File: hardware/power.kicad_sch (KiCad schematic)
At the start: 27 parts, among them J7 12401610E4#2A, Q1 DMG2307L, Q2 DMG2307L, Q3 BSD235N, U7 AP9101CK, U8 MIC5504-3.3YM5

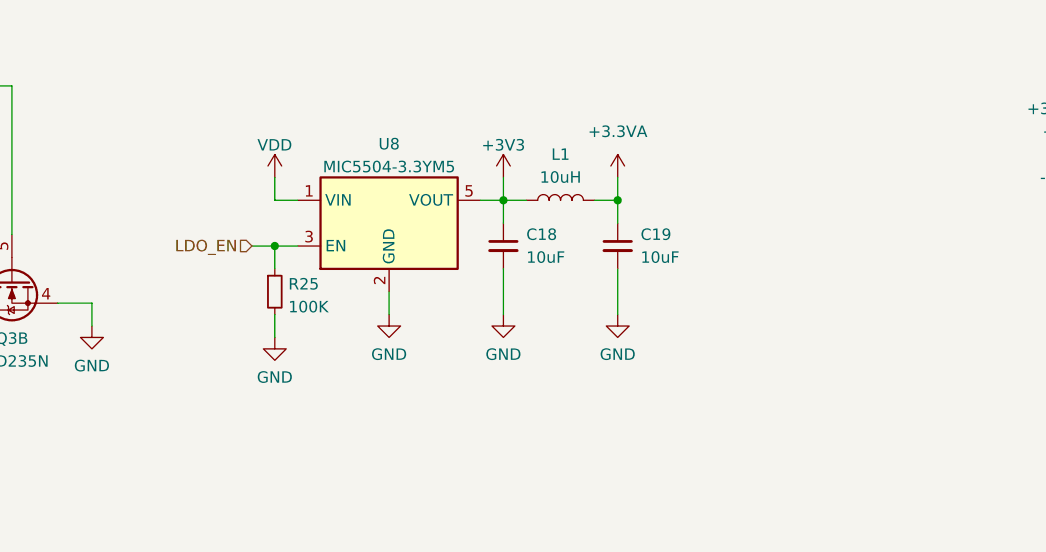
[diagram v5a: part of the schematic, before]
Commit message: Added solder bridges and calculated resistor values for INA
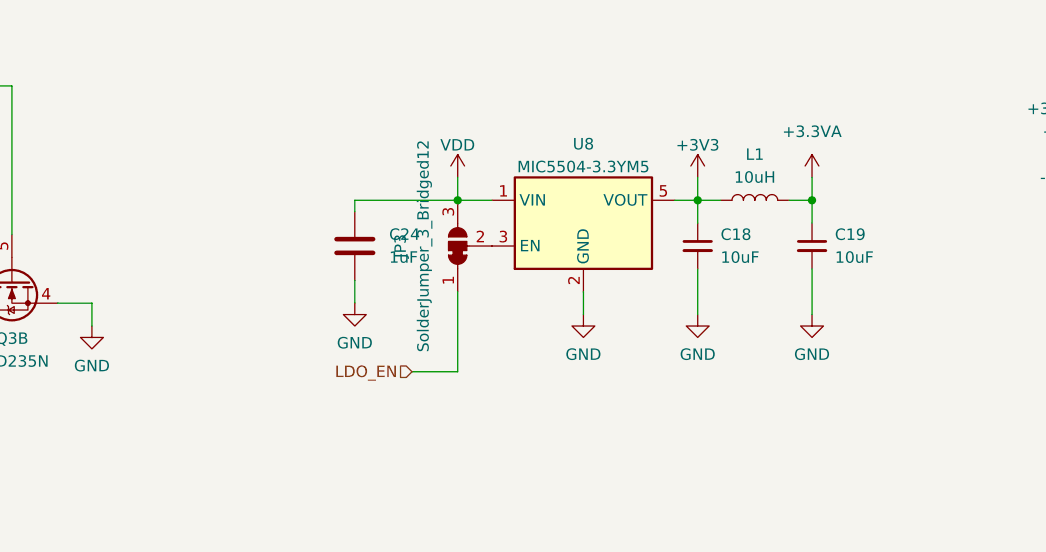
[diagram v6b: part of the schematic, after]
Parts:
- removed R25: 100K, Resistor_SMD:R_0603_1608Metric, symbol Device:R_Small
- added C24: 1uF, Capacitor_SMD:C_0603_1608Metric, symbol Device:C
- added JP3: SolderJumper_3_Bridged12, symbol Jumper:SolderJumper_3_Bridged12
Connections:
- net +BATT: now also C24.2, JP3.3 (B)
- net GND: now also C24.1
- net LDO_EN: now also JP3.1 (A); no longer U8.3 (EN)
- new net: JP3.2 (C), U8.3 (EN)
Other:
- moved on the sheet: C18, C19, L1, U8

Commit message: Set jumper footprints and updated design rules for Oshpark After Dark
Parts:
- JP3: footprint (none) -> Jumper:SolderJumper-3_P1.3mm_Bridged2Bar12_RoundedPad1.0x1.5mm
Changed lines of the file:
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@@
 			)
 		)
-		(property "Footprint" ""
+		(property "Footprint" "Jumper:SolderJumper-3_P1.3mm_Bridged2Bar12_RoundedPad1.0x1.5mm"
 			(at 193.04 36.83 0)
 			(effects

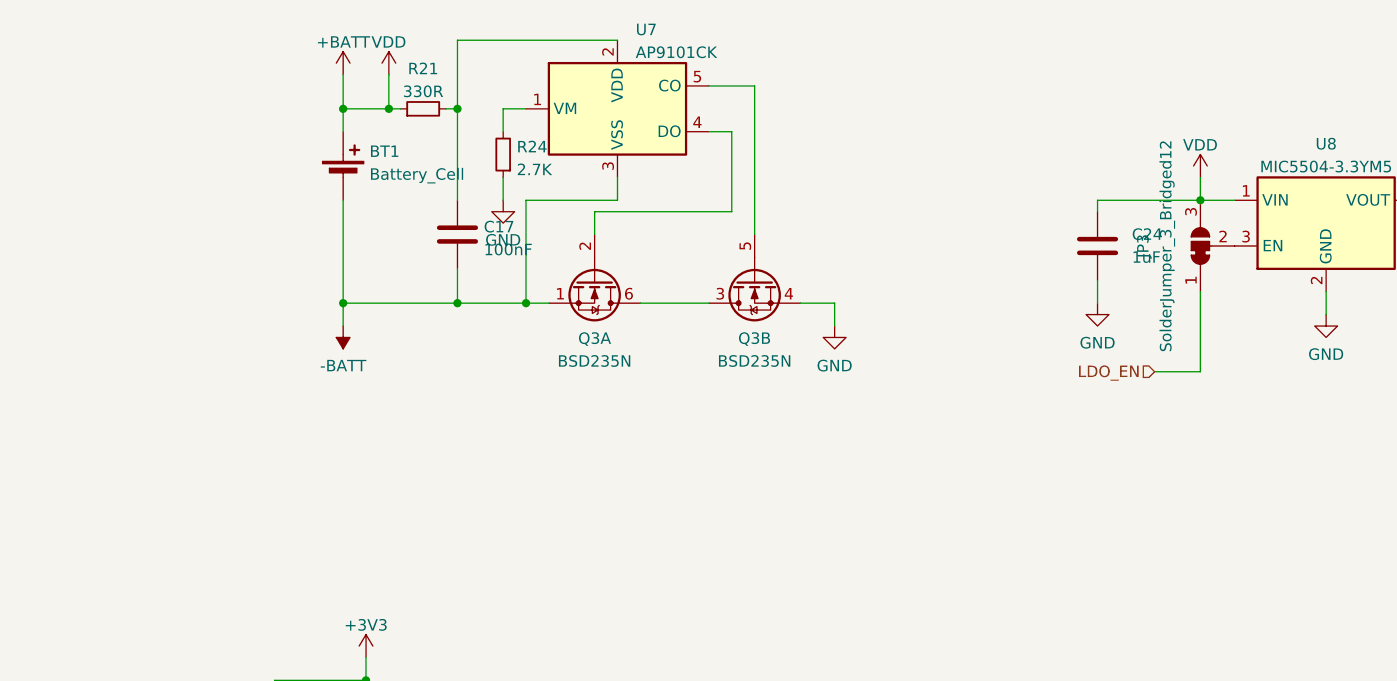
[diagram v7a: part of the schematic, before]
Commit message: Realized that 5V to VBat pin would fry the uC and abandoned ultra-low power design. Deferred to next revision.
A
A
A
A
A
A
A
A
A
A
A
A
A
A
A
A
A
A
B
B
B
B
B
B
B
B
B
B
B
B
B
B
B
A
A
A
A
A
A
A
A
A
A
A
A
A
A
P
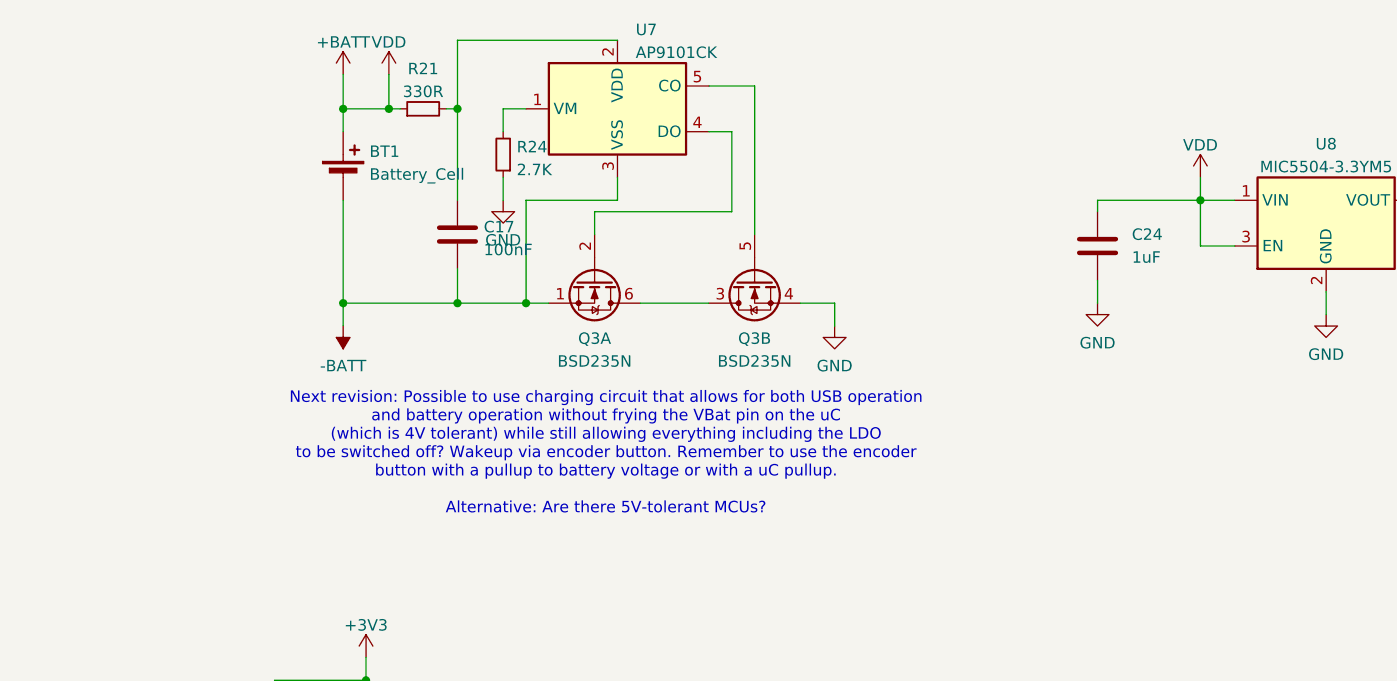
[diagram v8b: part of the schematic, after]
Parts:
- removed JP3: SolderJumper_3_Bridged12, Jumper:SolderJumper-3_P1.3mm_Bridged2Bar12_RoundedPad1.0x1.5mm, symbol Jumper:SolderJumper_3_Bridged12
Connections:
- net +BATT: now also U8.3 (EN)
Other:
- note added: "Next revision: Possible to use charging circuit that allows for both USB operation and battery operation without frying the VBat pin on the uC (which is 4V tolerant) while still allowing everything including the LDO to be switched off? Wakeup via encoder button. Remember to use the encoder button with a pullup to battery voltage or with a uC pullup. Alternative: Are there 5V-tolerant MCUs?"
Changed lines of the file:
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@@
 	(generator_version "9.0")
 	(paper "A4")
+	(text "Next revision: Possible to use charging circuit that allows for both USB operation \nand battery operation without frying the VBat pin on the uC \n(which is 4V tolerant) while still allowing everything including the LDO \nto be switched off? Wakeup via encoder button. Remember to use the encoder \nbutton with a pullup to battery voltage or with a uC pullup. \n\nAlternative: Are there 5V-tolerant MCUs?"
+		(exclude_from_sim no)
+		(at 127 59.944 0)
+		(effects
+			(font
+				(size 1.27 1.27)
+			)
+		)
+	)
 	(junction
 		(at 193.04 31.75)
@@
 	(wire
 		(pts
-			(xy 193.04 41.91) (xy 193.04 50.8)
-		)
-		(stroke
-			(width 0)
-			(type default)
-		)
-	)
-	(wire
-		(pts
 			(xy 140.97 33.02) (xy 125.73 33.02)
 		)
@@
 	(wire
 		(pts
+			(xy 193.04 36.83) (xy 193.04 31.75)
+		)
+		(stroke
+			(width 0)
+			(type default)
+		)
+	)
+	(wire
+		(pts
 			(xy 110.49 39.37) (xy 110.49 43.18)
 		)
@@
 	(wire
 		(pts
-			(xy 138.43 19.05) (xy 143.51 19.05)
+			(xy 196.85 36.83) (xy 193.04 36.83)
 		)
 		(stroke
@@
 	(wire
 		(pts
-			(xy 138.43 24.13) (xy 140.97 24.13)
+			(xy 138.43 19.05) (xy 143.51 19.05)
 		)
 		(stroke
@@
 	(wire
 		(pts
-			(xy 207.01 41.91) (xy 207.01 44.45)
+			(xy 138.43 24.13) (xy 140.97 24.13)
 		)
 		(stroke
@@
 	(wire
 		(pts
-			(xy 90.17 132.08) (xy 90.17 129.54)
+			(xy 207.01 41.91) (xy 207.01 44.45)
 		)
 		(stroke
@@
 	(wire
 		(pts
-			(xy 181.61 33.02) (xy 181.61 31.75)
+			(xy 90.17 132.08) (xy 90.17 129.54)
 		)
 		(stroke
@@
 	(wire
 		(pts
-			(xy 80.01 95.25) (xy 82.55 95.25)
+			(xy 181.61 33.02) (xy 181.61 31.75)
 		)
 		(stroke
@@
 	(wire
 		(pts
-			(xy 128.27 13.97) (xy 110.49 13.97)
+			(xy 80.01 95.25) (xy 82.55 95.25)
 		)
 		(stroke
@@
 	(wire
 		(pts
-			(xy 187.96 50.8) (xy 193.04 50.8)
+			(xy 128.27 13.97) (xy 110.49 13.97)
 		)
 		(stroke
@@
 		)
 	)
-	(hierarchical_label "LDO_EN"
-		(shape input)
-		(at 187.96 50.8 180)
-		(effects
-			(font
-				(size 1.27 1.27)
-			)
-			(justify right)
-		)
-	)
 	(hierarchical_label "DISPLAY_POWER"
 		(shape output)
@@
 					(unit 1)
 				)
-			)
-		)
-	)
-	(symbol
-		(lib_id "Jumper:SolderJumper_3_Bridged12")
-		(at 193.04 36.83 90)
-		(unit 1)
-		(exclude_from_sim no)
-		(in_bom no)
-		(on_board yes)
-		(dnp no)
-		(property "Reference" "JP3"
-			(at 186.69 36.83 0)
-			(effects
-				(font
-					(size 1.27 1.27)
-				)
-			)
-		)
-		(property "Value" "SolderJumper_3_Bridged12"
-			(at 189.23 36.83 0)
-			(effects
-				(font
-					(size 1.27 1.27)
-				)
-			)
-		)
-		(property "Footprint" "Jumper:SolderJumper-3_P1.3mm_Bridged2Bar12_RoundedPad1.0x1.5mm"
-			(at 193.04 36.83 0)
-			(effects
-				(font
-					(size 1.27 1.27)
-				)
-				(hide yes)
-			)
-		)
-		(property "Datasheet" "~"
-			(at 193.04 36.83 0)
-			(effects
-				(font
-					(size 1.27 1.27)
-				)
-				(hide yes)
-			)
-		)
-		(property "Description" "3-pole Solder Jumper, pins 1+2 closed/bridged"
-			(at 193.04 36.83 0)
-			(effects
-				(font
-					(size 1.27 1.27)
-				)
-				(hide yes)
-			)
-		)
-		(pin "1"
-		)
-		(pin "3"
-		)
-		(pin "2"
-		)
-		(instances
-			(project "Scale"
-				(path "/adf38c8f-bada-4838-acc6-e6af19946742/8a4812e6-01d2-4a59-bc73-706ba54f858f"
-					(reference "JP3")
-					(unit 1)
-				)
